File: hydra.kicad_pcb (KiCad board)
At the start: 4 copper layers, 95.9 x 90.2 mm, 61 parts, among them J1 PC104 Interconnect, J2 STLINK/V2 Header, J3 STLINK/V2 Clone Header, J5 UART Header, U2 AMS1117-3.3, U3 STM32F103VCTx, Y1 16mHz

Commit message: feat: trying multinodal
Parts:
- removed the J2 at (160.6, 40.4)
- removed Y1: 16mHz, Crystal:Crystal_HC49-U_Vertical
- added C15: 0.1uF, Capacitor_SMD:C_0603_1608Metric, F.Cu at (168.7, 46.8)
- added C16: 0.1uF, Capacitor_SMD:C_0603_1608Metric, F.Cu at (183.2, 54.6)
- added C17: 0.1uF, Capacitor_SMD:C_0603_1608Metric, F.Cu at (180.3, 60.0)
- added C18: 4.7uF, Capacitor_SMD:C_0603_1608Metric, F.Cu at (139.8, 84.6)
- added C19: 0.1uF, Capacitor_SMD:C_0603_1608Metric, F.Cu at (134.2, 78.3)
- added C20: 0.1uF, Capacitor_SMD:C_0603_1608Metric, F.Cu at (140.2, 90.6)
- added C21: 0.1uF, Capacitor_SMD:C_0603_1608Metric, F.Cu at (122.9, 90.2)
- added C22: 0.1uF, Capacitor_SMD:C_0603_1608Metric, F.Cu at (125.5, 79.8)
- added C23: 0.1uF, Capacitor_SMD:C_0603_1608Metric, F.Cu at (140.0, 87.7)
- added C24: 0.1uF, Capacitor_SMD:C_0603_1608Metric, F.Cu at (137.1, 93.0)
- added C25: 4.7uF, Capacitor_SMD:C_0603_1608Metric, F.Cu at (183.0, 84.6)
- added C26: 0.1uF, Capacitor_SMD:C_0603_1608Metric, F.Cu at (177.4, 78.3)
- added C27: 0.1uF, Capacitor_SMD:C_0603_1608Metric, F.Cu at (183.3, 90.6)
- added C28: 0.1uF, Capacitor_SMD:C_0603_1608Metric, F.Cu at (166.1, 90.2)
- added C29: 0.1uF, Capacitor_SMD:C_0603_1608Metric, F.Cu at (168.7, 79.8)
- added C30: 0.1uF, Capacitor_SMD:C_0603_1608Metric, F.Cu at (183.2, 87.7)
- added C31: 0.1uF, Capacitor_SMD:C_0603_1608Metric, F.Cu at (180.3, 93.0)
- added C32: 4.7uF, Capacitor_SMD:C_0603_1608Metric, F.Cu at (162.6, 110.0)
- added C33: 0.1uF, Capacitor_SMD:C_0603_1608Metric, F.Cu at (157.0, 103.7)
- added C34: 0.1uF, Capacitor_SMD:C_0603_1608Metric, F.Cu at (163.0, 116.0)
- added C35: 0.1uF, Capacitor_SMD:C_0603_1608Metric, F.Cu at (145.8, 115.6)
- added C36: 0.1uF, Capacitor_SMD:C_0603_1608Metric, F.Cu at (148.3, 105.2)
- added C37: 0.1uF, Capacitor_SMD:C_0603_1608Metric, F.Cu at (162.9, 113.1)
- added C38: 0.1uF, Capacitor_SMD:C_0603_1608Metric, F.Cu at (159.9, 118.4)
- added D15: Node Active LED, LED_SMD:LED_0603_1608Metric, F.Cu at (174.0, 45.8)
- added D16: Node Active LED, LED_SMD:LED_0603_1608Metric, F.Cu at (130.8, 78.8)
- added D17: Node Active LED, LED_SMD:LED_0603_1608Metric, F.Cu at (174.0, 78.8)
- added D18: Node Active LED, LED_SMD:LED_0603_1608Metric, F.Cu at (153.7, 104.2)
- added D2: CS1, LED_SMD:LED_0603_1608Metric, F.Cu at (68.1, 90.0)
- added J1: UART Header, Connector_PinHeader_2.54mm:PinHeader_1x03_P2.54mm_Vertical, F.Cu at (74.4, 101.4)
- added J4: STLINK/V2 Clone Header, Connector_PinHeader_2.54mm:PinHeader_2x05_P2.54mm_Vertical, F.Cu at (159.8, 49.8)
- added J6: STLINK/V2 Clone Header, Connector_PinHeader_2.54mm:PinHeader_2x05_P2.54mm_Vertical, F.Cu at (159.8, 82.8)
- added J7: STLINK/V2 Clone Header, Connector_PinHeader_2.54mm:PinHeader_2x05_P2.54mm_Vertical, F.Cu at (139.5, 108.2)
- added R18: 10K, Resistor_SMD:R_0603_1608Metric, F.Cu at (156.0, 121.1)
- added R19: 5.1K, Resistor_SMD:R_0603_1608Metric, F.Cu at (129.8, 43.1)
- added R2: 5.1K, Resistor_SMD:R_0603_1608Metric, F.Cu at (56.0, 97.4)
- added R20: 5.1K, Resistor_SMD:R_0603_1608Metric, F.Cu at (173.0, 43.1)
- added R21: 5.1K, Resistor_SMD:R_0603_1608Metric, F.Cu at (129.8, 76.2)
- added R22: 5.1K, Resistor_SMD:R_0603_1608Metric, F.Cu at (173.0, 76.2)
- added R23: 5.1K, Resistor_SMD:R_0603_1608Metric, F.Cu at (152.7, 101.6)
- added R3: 5.1K, Resistor_SMD:R_0603_1608Metric, F.Cu at (56.0, 99.9)
- added R4: 5.1K, Resistor_SMD:R_0603_1608Metric, F.Cu at (60.0, 87.4)
- added R5: 5.1K, Resistor_SMD:R_0603_1608Metric, F.Cu at (60.0, 89.9)
- added TP12: BOOT1 TP, TestPoint:TestPoint_Pad_D1.0mm, F.Cu at (169.6, 44.4)
- added TP13: BOOT1 TP, TestPoint:TestPoint_Pad_D1.0mm, F.Cu at (126.4, 77.4)
- added TP14: BOOT1 TP, TestPoint:TestPoint_Pad_D1.0mm, F.Cu at (169.6, 77.4)
- added TP15: BOOT1 TP, TestPoint:TestPoint_Pad_D1.0mm, F.Cu at (149.2, 102.8)
- added TP2: PSPI_MOSI_TP, TestPoint:TestPoint_Pad_D1.0mm, F.Cu at (67.5, 103.6)
- added U1: AMS1117-3.3, Package_TO_SOT_SMD:SOT-223-3_TabPin2, F.Cu at (58.9, 105.3)
- added U4: STM32L151RCTx, Package_QFP:LQFP-64_10x10mm_P0.5mm, F.Cu at (131.3, 86.9)
- added U5: STM32L151RCTx, Package_QFP:LQFP-64_10x10mm_P0.5mm, F.Cu at (174.5, 86.9)
- added U6: STM32L151RCTx, Package_QFP:LQFP-64_10x10mm_P0.5mm, F.Cu at (154.2, 112.3)
- C1: value 10uF -> 4.7uF
- C11, C4: value 0.1uF -> 4.7uF
- C2: value 22uF -> 10uF
- C3: value 4.7uF -> 22uF
- C7, C8: value 20pF -> 0.1uF
- D10: value CS8 -> CS9
- D11: value CS9 -> CS10
- D12: value CS10 -> CS11
- D13: value CS11 -> CS12
- D14: value CS12 -> Node Active LED
- D3: value CS1 -> CS2
- D4: value CS2 -> CS3
- D5: value CS3 -> CS4
- D6: value CS4 -> CS5
- D7: value CS5 -> CS6
- D8: value CS6 -> CS7
- D9: value CS7 -> CS8
- J5: value UART Header -> STLINK/V2 Clone Header; footprint Connector_PinHeader_2.54mm:PinHeader_1x03_P2.54mm_Vertical -> Connector_PinHeader_2.54mm:PinHeader_2x05_P2.54mm_Vertical
- R13: footprint Resistor_SMD:R_0603_1608Metric -> Capacitor_SMD:C_0603_1608Metric
- R14, R15, R16: value 5.1K -> 10K
- R17: value 5.1K -> 10K; footprint Capacitor_SMD:C_0603_1608Metric -> Resistor_SMD:R_0603_1608Metric
- TP10: value RSPI_MISO_TP -> RSPI_SCLK_TP
- TP11: value RSPI_SCLK_TP -> BOOT1 TP
- TP3: value PSPI_MOSI_TP -> PSPI_MISO_TP
- TP4: value PSPI_MISO_TP -> PSPI_SCLK_TP
- TP5: value PSPI_SCLK_TP -> SSPI_MOSI_TP
- TP6: value SSPI_MOSI_TP -> SSPI_MISO_TP
- TP7: value SSPI_MISO_TP -> SSPI_SCLK_TP
- TP8: value SSPI_SCLK_TP -> RSPI_MOSI_TP
- TP9: value RSPI_MOSI_TP -> RSPI_MISO_TP
- U2: value AMS1117-3.3 -> STM32L151RCTx; footprint Package_TO_SOT_SMD:SOT-223-3_TabPin2 -> Package_QFP:LQFP-64_10x10mm_P0.5mm
- U3: value STM32F103VCTx -> STM32L151RCTx; footprint Package_QFP:LQFP-100_14x14mm_P0.5mm -> Package_QFP:LQFP-64_10x10mm_P0.5mm
- moved R6 140.4 mm to (60.0, 92.4), turned to 0 degrees
- moved C1 134.2 mm to (56.0, 87.4), turned to 0 degrees
- moved D3 131.4 mm to (68.1, 92.6), turned to 0 degrees
- moved R1 120.7 mm to (56.0, 94.9), turned to 0 degrees
- moved TP9 119.7 mm to (70.6, 109.7)
- moved C2 119.7 mm to (56.0, 89.9), turned to 0 degrees
- moved TP6 119.1 mm to (70.6, 100.6)
- moved TP10 116.9 mm to (70.6, 112.8)
- moved TP7 113.4 mm to (70.6, 103.6)
- moved D1 110.1 mm to (68.1, 87.4), turned to 0 degrees
- moved TP8 108.7 mm to (70.6, 106.7)
- moved R9 108.3 mm to (60.0, 99.9)
- moved TP1 107.1 mm to (67.5, 100.6)
- moved TP5 100.2 mm to (67.5, 112.8)
- moved TP3 94.7 mm to (67.5, 106.7)
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- renumbered H3 to H2, H2 to H3, J1 to J2
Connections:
- C1 pad 1: /3V3_CONN -> +3V3
- C2 pad 1: +3V3 -> /3V3_CONN
- C7 pad 1: GND -> +3V3
- C7 pad 2: /OSC+ -> GND
- C8 pad 1: GND -> +3V3
- C8 pad 2: /OSC- -> GND
- C9 pad 1: /RESET -> /Node/RESET
- D10 pad 2: /CS_8 -> /CS_9
- D11 pad 2: /CS_9 -> /CS_10
- D12 pad 2: /CS_10 -> /CS_11
- D13 pad 2: /CS_11 -> /CS_12
- D14 pad 2: /CS_12 -> Net-(D14-A)
- D3 pad 2: /CS_1 -> /CS_2
- D4 pad 2: /CS_2 -> /CS_3
- D5 pad 2: /CS_3 -> /CS_4
- D6 pad 2: /CS_4 -> /CS_5
- D7 pad 2: /CS_5 -> /CS_6
- D8 pad 2: /CS_6 -> /CS_7
- D9 pad 2: /CS_7 -> /CS_8
- J2 pad 32: /JTDO/R_SCLK -> /R_SCLK
- J2 pad 34: /NJTRST/R_MISO -> /R_MISO
- J3 pad 1: /RESET -> /Node/RESET
- J3 pad 2: GND -> /Node/SWDIO
- J3 pad 3: /SWIM -> GND
- J3 pad 4: +3V3 -> GND
- J3 pad 6: /JTMS/SWDIO -> /Node/SWCLK
- J3 pad 7: GND -> +3V3
- J3 pad 8: /JTCK/SWCLK -> +3V3
- J3 pad 9: +3V3 -> unconnected-(J3-Pin_9-Pad9)
- J5 pad 1: /USART_RX -> /Node2/RESET
- J5 pad 2: /USART_TX -> /Node2/SWDIO
- R10 pad 2: Net-(D7-K) -> Net-(D10-K)
- R11 pad 2: Net-(D8-K) -> Net-(D11-K)
- R12 pad 2: Net-(D9-K) -> Net-(D12-K)
- R13 pad 2: Net-(D10-K) -> Net-(D13-K)
- R14 pad 2: Net-(D11-K) -> Net-(U2-BOOT0)
- R15 pad 2: Net-(D12-K) -> Net-(U3-BOOT0)
- R16 pad 2: Net-(D13-K) -> Net-(U4-BOOT0)
- R17 pad 2: Net-(D14-K) -> Net-(U5-BOOT0)
- R6 pad 2: Net-(D3-K) -> Net-(D6-K)
- R7 pad 2: Net-(D4-K) -> Net-(D7-K)
- R8 pad 2: Net-(D5-K) -> Net-(D8-K)
- R9 pad 2: Net-(D6-K) -> Net-(D9-K)
- TP10 pad 1: /NJTRST/R_MISO -> /R_SCLK
- TP11 pad 1: /JTDO/R_SCLK -> /Node/BOOT1
- TP3 pad 1: /P_MOSI -> /P_MISO
- TP4 pad 1: /P_MISO -> /P_SCLK
- TP5 pad 1: /P_SCLK -> /S_MOSI
- TP6 pad 1: /S_MOSI -> /S_MISO
- TP7 pad 1: /S_MISO -> /S_SCLK
- TP8 pad 1: /S_SCLK -> /R_MOSI
- TP9 pad 1: /R_MOSI -> /R_MISO
- U2 pad 1: GND -> +3V3
- U2 pad 2: +3V3 -> /CS_12
- U2 pad 3: /3V3_CONN -> /CS_11
- U3 pad 1: unconnected-(U3-PE2-Pad1) -> +3V3
- U3 pad 10: GND -> /CS_7
- U3 pad 11: +3V3 -> /CS_6
- U3 pad 12: /OSC+ -> GND
- U3 pad 13: /OSC- -> +3V3
- U3 pad 14: /RESET -> /CS_5
- U3 pad 15: unconnected-(U3-PC0-Pad15) -> /CS_4
- U3 pad 16: unconnected-(U3-PC1-Pad16) -> /CS_3
- U3 pad 17: unconnected-(U3-PC2-Pad17) -> /CS_2
- U3 pad 18: unconnected-(U3-PC3-Pad18) -> GND
- U3 pad 19: GND -> +3V3
- U3 pad 2: unconnected-(U3-PE3-Pad2) -> /CS_12
- U3 pad 20: GND -> /CS_1
- U3 pad 21: +3V3 -> /P_SCLK
- U3 pad 22: +3V3 -> /P_MISO
- U3 pad 23: unconnected-(U3-PA0-Pad23) -> /P_MOSI
- U3 pad 24: unconnected-(U3-PA1-Pad24) -> Net-(D15-A)
- U3 pad 27: GND -> unconnected-(U3-PB1-Pad27)
- U3 pad 28: +3V3 -> /Node1/BOOT1
- U3 pad 3: unconnected-(U3-PE4-Pad3) -> /CS_11
- U3 pad 30: /P_SCLK -> unconnected-(U3-PB11-Pad30)
- U3 pad 31: /P_MISO -> GND
- U3 pad 32: /P_MOSI -> +3V3
- U3 pad 34: unconnected-(U3-PC5-Pad34) -> /S_SCLK
- U3 pad 35: unconnected-(U3-PB0-Pad35) -> /S_MISO
- U3 pad 36: unconnected-(U3-PB1-Pad36) -> /S_MOSI
- U3 pad 4: unconnected-(U3-PE5-Pad4) -> /CS_10
- U3 pad 46: unconnected-(U3-PE15-Pad46) -> /Node1/SWDIO
- U3 pad 47: unconnected-(U3-PB10-Pad47) -> GND
- U3 pad 48: unconnected-(U3-PB11-Pad48) -> +3V3
- U3 pad 49: GND -> /Node1/SWCLK
- U3 pad 50: +3V3 -> unconnected-(U3-PA15-Pad50)
- U3 pad 51: unconnected-(U3-PB12-Pad51) -> /R_SCLK
- U3 pad 52: /S_SCLK -> /R_MISO
- U3 pad 53: /S_MISO -> /R_MOSI
- U3 pad 54: /S_MOSI -> /R_CS
- U3 pad 55: /R_CS -> /Node1/JTDO
- U3 pad 56: /CS_12 -> /Node1/NJTRST
- U3 pad 57: /CS_11 -> unconnected-(U3-PB5-Pad57)
- U3 pad 58: /CS_10 -> /USART_TX
- U3 pad 59: /CS_9 -> /USART_RX
- U3 pad 6: +3V3 -> unconnected-(U3-PH1-Pad6)
- U3 pad 60: /CS_8 -> Net-(U3-BOOT0)
- U3 pad 61: /CS_7 -> /INTRA_SCL
- U3 pad 62: /CS_6 -> /INTRA_SDA
- U3 pad 63: /CS_5 -> GND
- U3 pad 64: /CS_4 -> +3V3
- U3 pad 7: unconnected-(U3-PC13-Pad7) -> /Node1/RESET
- U3 pad 8: unconnected-(U3-PC14-Pad8) -> /CS_9
- U3 pad 9: unconnected-(U3-PC15-Pad9) -> /CS_8
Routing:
- net /S_MOSI: track 55.0 -> 192.6 mm, vias 2 -> 12
- net /S_MISO: track 57.1 -> 193.2 mm, vias 2 -> 13
- net /S_SCLK: track 55.7 -> 191.6 mm, vias 3 -> 12
- net /P_SCLK: track 65.4 -> 179.8 mm, vias 0 -> 5
- net /NJTRST/R_MISO: track 112.8 -> 0.00 mm, vias 3 -> 0
- net /JTDO/R_SCLK: track 109.9 -> 0.00 mm, vias 4 -> 0
- net /P_MOSI: track 63.0 -> 170.9 mm, vias 0 -> 8
- net /P_MISO: track 66.7 -> 172.2 mm, vias 0 -> 7
- net /RESET: track 86.7 -> 0.00 mm
- net GND: track 18.7 -> 98.6 mm, vias 48 -> 46
- net /JTCK/SWCLK: track 69.1 -> 0.00 mm, vias 2 -> 0
- net /R_CS: track 69.0 -> 0.00 mm
- net /R_MOSI: track 66.9 -> 0.00 mm, vias 2 -> 0
- net /JTMS/SWDIO: track 66.0 -> 0.00 mm
- net /CS_12: track 56.6 -> 118.1 mm, vias 0 -> 1
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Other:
- board text removed: "(0, 0) local"
- board text removed: "(205, 125) world"

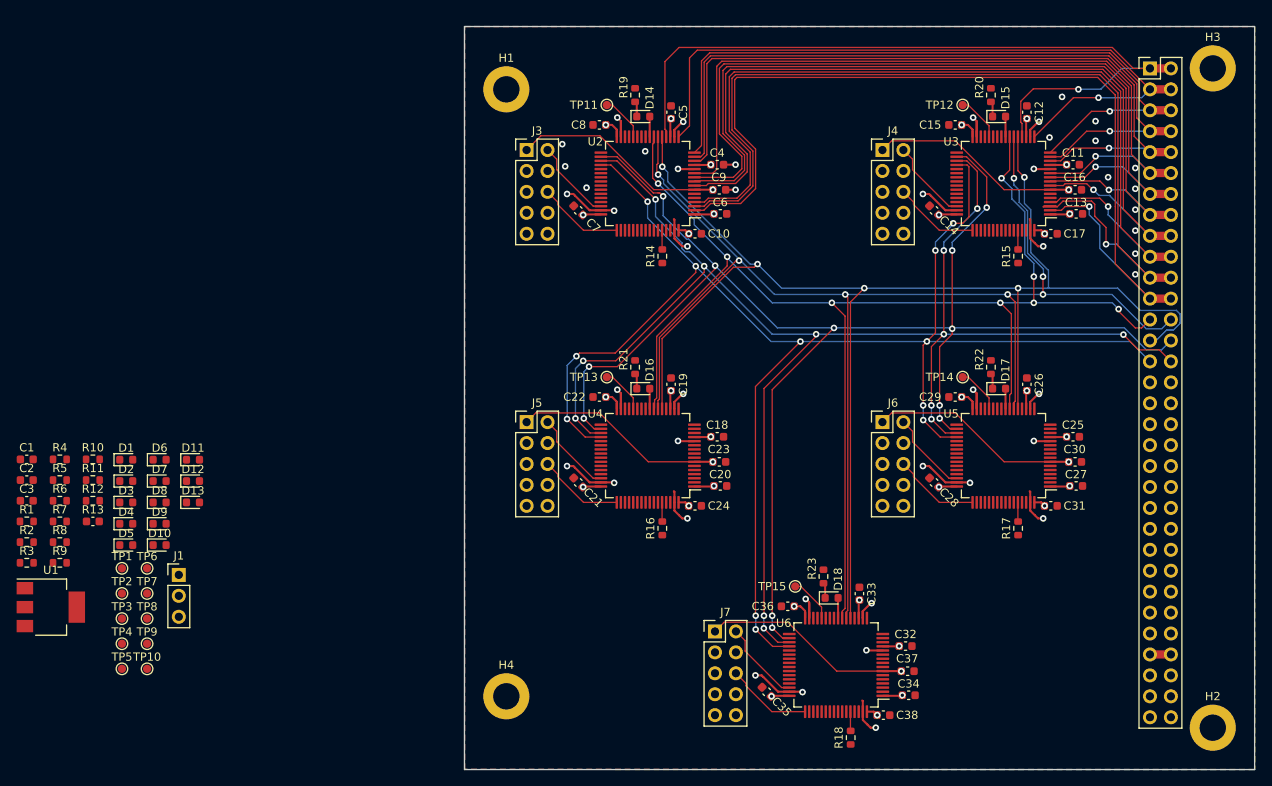
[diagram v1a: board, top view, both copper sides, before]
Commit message: feat: more routing
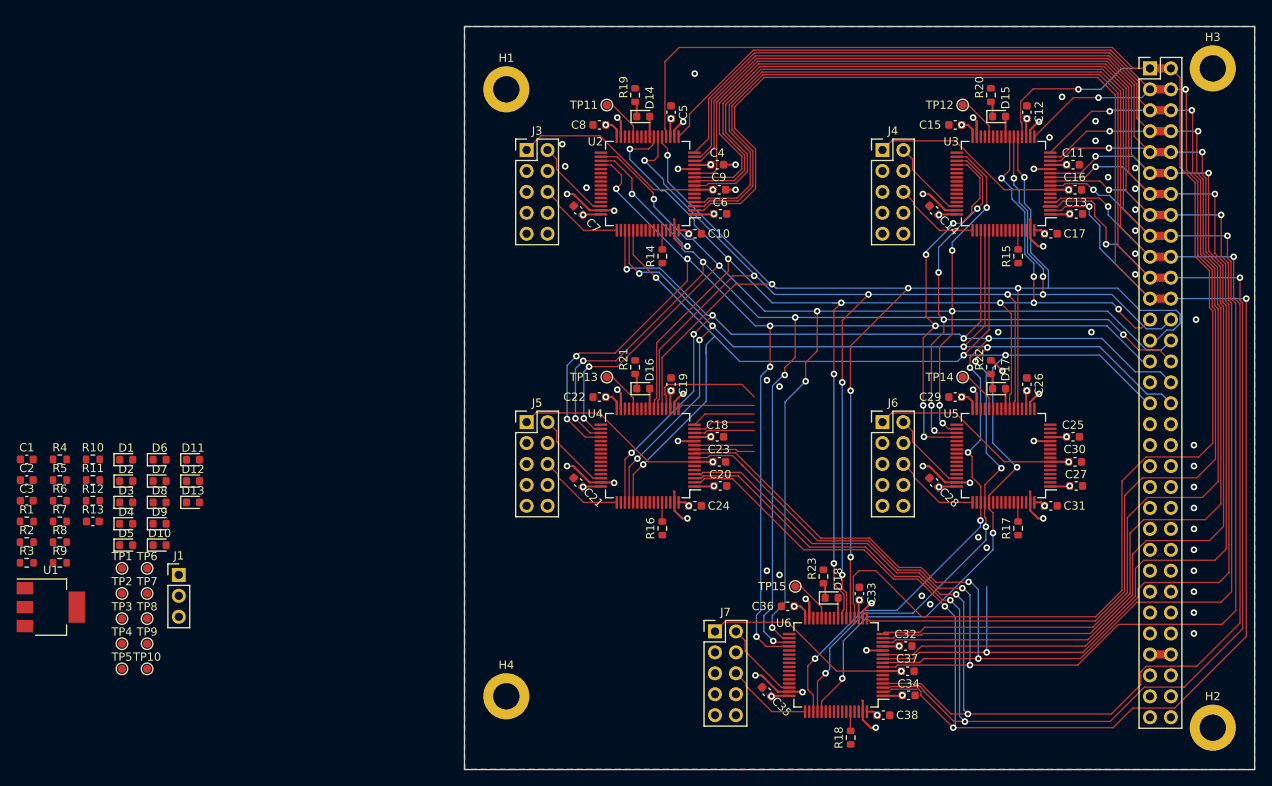
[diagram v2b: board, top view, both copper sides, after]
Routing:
- net /R_SCLK: track 0.00 -> 177.2 mm, vias 0 -> 10
- net /R_MISO: track 0.00 -> 176.8 mm, vias 0 -> 10
- net /R_MOSI: track 0.00 -> 174.7 mm, vias 0 -> 7
- net /CS_10: track 110.4 -> 264.3 mm, vias 1 -> 4
- net /CS_12: track 118.1 -> 271.1 mm, vias 1 -> 4
- net /CS_11: track 116.8 -> 269.4 mm, vias 1 -> 4
- net /CS_8: track 103.0 -> 248.8 mm, vias 1 -> 4
- net /CS_9: track 106.0 -> 251.5 mm, vias 1 -> 4
- net /CS_1: track 94.1 -> 223.8 mm
- net /CS_7: track 101.1 -> 213.4 mm, vias 1 -> 3
- net /CS_2: track 87.3 -> 198.3 mm, vias 1 -> 2
- net /CS_3: track 87.2 -> 194.4 mm, vias 1 -> 2
- net /CS_4: track 89.0 -> 195.3 mm, vias 1 -> 2
- net /CS_5: track 90.8 -> 195.4 mm, vias 1 -> 2
- net /CS_6: track 95.2 -> 199.7 mm, vias 1 -> 2
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- added copper zone on B.Cu, net +3V3
- added copper zone on In2.Cu, net GND
- removed copper zone on In2.Cu, net +3V3
- removed copper zone on B.Cu, net GND

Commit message: feat: mostly put together multinode
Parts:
- added G***: LOGO, mod:hsl, F.Cu at (126.8, 107.5)
- added kibuzzard-65E1979C: G***, kibuzzard-65E1979C, F.Cu at (138.8, 47.8)
- added kibuzzard-65E197AB: G***, kibuzzard-65E197AB, F.Cu at (182.3, 46.9)
- added kibuzzard-65E197B8: G***, kibuzzard-65E197B8, F.Cu at (138.2, 80.8)
- added kibuzzard-65E197C4: G***, kibuzzard-65E197C4, F.Cu at (182.5, 80.9)
- added kibuzzard-65E197D2: G***, kibuzzard-65E197D2, F.Cu at (161.6, 106.2)
- added kibuzzard-65E19948: G***, kibuzzard-65E19948, F.Cu at (127.0, 117.6)
- moved C2 135.0 mm to (189.5, 110.2), turned to 90 degrees
- moved U1 125.3 mm to (183.9, 113.3), turned to 180 degrees
- moved C3 124.4 mm to (178.7, 112.6), turned to 90 degrees
- moved TP10 123.8 mm to (189.0, 76.7)
- moved TP9 119.4 mm to (185.2, 76.1)
- moved TP8 114.3 mm to (180.4, 74.7)
- moved TP7 105.5 mm to (168.3, 63.8)
- moved TP4 101.8 mm to (160.8, 68.9)
- moved TP3 96.4 mm to (156.4, 69.1)
- moved TP2 91.7 mm to (153.9, 73.1)
- moved TP5 87.5 mm to (146.2, 74.5)
- moved TP6 83.3 mm to (149.2, 73.1)
- moved C1 4.40 mm to (56.1, 83.0)
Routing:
- net /INTRA_SCL: track 0.00 -> 209.4 mm, vias 0 -> 13
- net /INTRA_SDA: track 0.00 -> 208.3 mm, vias 0 -> 10
- net /R_CS: track 0.00 -> 160.4 mm, vias 0 -> 9
- net /CS_1: track 223.8 -> 295.2 mm
- net /CS_2: track 198.3 -> 263.3 mm, vias 2 -> 6
- net /CS_5: track 195.4 -> 259.0 mm, vias 2 -> 6
- net /CS_4: track 195.3 -> 258.2 mm, vias 2 -> 6
- net /CS_3: track 194.4 -> 256.5 mm, vias 2 -> 6
- net /CS_6: track 199.7 -> 259.7 mm, vias 2 -> 6
- net /CS_7: track 213.4 -> 264.9 mm, vias 3 -> 6
- net /CS_12: track 271.1 -> 297.3 mm, vias 4 -> 6
- net /CS_11: track 269.4 -> 294.9 mm, vias 4 -> 6
- net /CS_10: track 264.3 -> 289.4 mm, vias 4 -> 6
- net /CS_9: track 251.5 -> 272.7 mm, vias 4 -> 6
- net /CS_8: track 248.8 -> 266.7 mm, vias 4 -> 6
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- added copper zone on In2.Cu, net +3V3
- added copper zone on B.Cu, net GND
- removed copper zone on B.Cu, net +3V3
- removed copper zone on In2.Cu, net GND

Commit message: feat: in progress rework
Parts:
- removed C1, C11, C18, C25, C32: 4.7uF, Capacitor_SMD:C_0603_1608Metric
- removed C12, C13, C14, C15, C16, C17, C19, C20, C21, C22, C23, C24, C26, C27, C28, C29, C30, C31, C33, C34, C35, C36, C37, C38: 0.1uF, Capacitor_SMD:C_0603_1608Metric
- removed D10: CS9, LED_SMD:LED_0603_1608Metric
- removed D11: CS10, LED_SMD:LED_0603_1608Metric
- removed D12: CS11, LED_SMD:LED_0603_1608Metric
- removed D13: CS12, LED_SMD:LED_0603_1608Metric
- removed D14, D15, D16, D17, D18: Node Active LED, LED_SMD:LED_0603_1608Metric
- removed D2: CS1, LED_SMD:LED_0603_1608Metric
- removed D3: CS2, LED_SMD:LED_0603_1608Metric
- removed D4: CS3, LED_SMD:LED_0603_1608Metric
- removed D5: CS4, LED_SMD:LED_0603_1608Metric
- removed D6: CS5, LED_SMD:LED_0603_1608Metric
- removed D7: CS6, LED_SMD:LED_0603_1608Metric
- removed D8: CS7, LED_SMD:LED_0603_1608Metric
- removed D9: CS8, LED_SMD:LED_0603_1608Metric
- removed J1: UART Header, Connector_PinHeader_2.54mm:PinHeader_1x03_P2.54mm_Vertical
- removed J4, J5, J6, J7: STLINK/V2 Clone Header, Connector_PinHeader_2.54mm:PinHeader_2x05_P2.54mm_Vertical
- removed R10, R11, R12, R19, R2, R20, R21, R22, R23, R3, R4, R5, R6, R7, R8, R9: 5.1K, Resistor_SMD:R_0603_1608Metric
- removed R13: 5.1K, Capacitor_SMD:C_0603_1608Metric
- removed R14, R15, R16, R17, R18: 10K, Resistor_SMD:R_0603_1608Metric
- removed TP12, TP13, TP14, TP15: BOOT1 TP, TestPoint:TestPoint_Pad_D1.0mm
- removed U4, U5, U6: STM32L151RCTx, Package_QFP:LQFP-64_10x10mm_P0.5mm
- removed kibuzzard-65E1979C: G***, kibuzzard-65E1979C
- removed kibuzzard-65E197AB: G***, kibuzzard-65E197AB
- removed kibuzzard-65E197B8: G***, kibuzzard-65E197B8
- removed kibuzzard-65E197C4: G***, kibuzzard-65E197C4
- removed kibuzzard-65E197D2: G***, kibuzzard-65E197D2
- added J8: TC2030, Connector:Tag-Connect_TC2030-IDC-FP_2x03_P1.27mm_Vertical, F.Cu at (166.6, 47.0)
- J3: value STLINK/V2 Clone Header -> USB-C; footprint Connector_PinHeader_2.54mm:PinHeader_2x05_P2.54mm_Vertical -> Connector_USB:USB_C_Receptacle_G-Switch_GT-USB-7010ASV
- U2: value STM32L151RCTx -> STM32L151RCT6
- U3: value STM32L151RCTx -> USBLC6-2SC6; footprint Package_QFP:LQFP-64_10x10mm_P0.5mm -> Package_TO_SOT_SMD:SOT-23-6
- moved C2 84.1 mm to (122.4, 59.4), turned to 0 degrees
- moved C3 75.7 mm to (122.4, 61.9), turned to 0 degrees
- moved R1 73.1 mm to (122.4, 64.4)
- moved D1 72.1 mm to (134.5, 59.4)
- moved TP1 72.1 mm to (134.0, 72.6)
- moved U1 68.7 mm to (125.4, 77.4), turned to 0 degrees
- moved J3 59.3 mm to (174.7, 37.5), turned to 180 degrees
- moved TP10 52.6 mm to (137.0, 84.8)
- moved TP9 48.5 mm to (137.0, 81.8)
- moved U2 45.3 mm to (176.6, 55.8), turned to 90 degrees
- moved TP8 43.5 mm to (137.0, 78.7)
- moved TP5 42.9 mm to (187.5, 62.9)
- moved C5 41.9 mm to (172.0, 63.3), turned to 180 degrees
- moved TP11 39.4 mm to (148.1, 77.2)
- moved TP2 39.0 mm to (181.0, 44.9)
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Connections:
- U2 pad 10: /CS_7 -> unconnected-(U2-PC2-Pad10)
- U2 pad 11: /CS_6 -> /R_CS
- U2 pad 14: /CS_5 -> /CS_12
- U2 pad 15: /CS_4 -> /CS_11
- U2 pad 16: /CS_3 -> /CS_10
- U2 pad 17: /CS_2 -> /CS_9
- U2 pad 2: /CS_12 -> unconnected-(U2-PC13-Pad2)
- U2 pad 20: /CS_1 -> /CS_8
- U2 pad 21: /P_SCLK -> /S_SCLK
- U2 pad 22: /P_MISO -> /S_MISO
- U2 pad 23: /P_MOSI -> /S_MOSI
- U2 pad 24: Net-(D14-A) -> /CS_7
- U2 pad 25: unconnected-(U2-PC5-Pad25) -> /CS_6
- U2 pad 26: unconnected-(U2-PB0-Pad26) -> /CS_5
- U2 pad 27: unconnected-(U2-PB1-Pad27) -> /CS_4
- U2 pad 29: unconnected-(U2-PB10-Pad29) -> /CS_3
- U2 pad 3: /CS_11 -> unconnected-(U2-PC14-Pad3)
- U2 pad 30: unconnected-(U2-PB11-Pad30) -> /CS_2
- U2 pad 33: unconnected-(U2-PB12-Pad33) -> /CS_1
- U2 pad 34: /S_SCLK -> /P_SCLK
- U2 pad 35: /S_MISO -> /P_MISO
- U2 pad 36: /S_MOSI -> /P_MOSI
- U2 pad 4: /CS_10 -> unconnected-(U2-PC15-Pad4)
- U2 pad 44: unconnected-(U2-PA11-Pad44) -> /Node/USB_D-
- U2 pad 45: unconnected-(U2-PA12-Pad45) -> /Node/USB_D+
- U2 pad 46: /Node/SWDIO -> /Node/SWD_IO
- U2 pad 49: /Node/SWCLK -> /Node/SWD_CLK
- U2 pad 5: unconnected-(U2-PH0-Pad5) -> /Node/HSE+
- U2 pad 54: /R_CS -> unconnected-(U2-PD2-Pad54)
- U2 pad 55: /Node/JTDO -> unconnected-(U2-PB3-Pad55)
- U2 pad 56: /Node/NJTRST -> unconnected-(U2-PB4-Pad56)
- U2 pad 58: /USART_TX -> /Node/UART_RX
- U2 pad 59: /USART_RX -> /Node/UART_TX
- U2 pad 6: unconnected-(U2-PH1-Pad6) -> /Node/HSE-
- U2 pad 60: Net-(U2-BOOT0) -> /Node/BOOT0
- U2 pad 8: /CS_9 -> unconnected-(U2-PC0-Pad8)
- U2 pad 9: /CS_8 -> unconnected-(U2-PC1-Pad9)
- U3 pad 1: +3V3 -> /Node/USB_DT-
- U3 pad 2: /CS_12 -> GND
- U3 pad 3: /CS_11 -> /Node/USB_DT+
- U3 pad 4: /CS_10 -> /Node/USB_D+
- U3 pad 5: unconnected-(U3-PH0-Pad5) -> Net-(U3-VBUS)
- U3 pad 6: unconnected-(U3-PH1-Pad6) -> /Node/USB_D-
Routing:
- net /CS_12: track 297.3 -> 19.3 mm, vias 6 -> 1
- net /CS_11: track 294.9 -> 17.6 mm, vias 6 -> 1
- net /CS_1: track 295.2 -> 18.8 mm
- net /CS_10: track 289.4 -> 15.9 mm, vias 6 -> 1
- net /CS_9: track 272.7 -> 12.8 mm, vias 6 -> 1
- net /CS_8: track 266.7 -> 13.3 mm, vias 6 -> 1
- net /CS_7: track 264.9 -> 12.9 mm, vias 6 -> 1
- net /CS_6: track 259.7 -> 13.8 mm, vias 6 -> 1
- net /CS_2: track 263.3 -> 18.5 mm, vias 6 -> 1
- net /CS_5: track 259.0 -> 14.6 mm, vias 6 -> 1
- net /CS_4: track 258.2 -> 15.5 mm, vias 6 -> 1
- net /CS_3: track 256.5 -> 17.3 mm, vias 6 -> 1
- net /INTRA_SCL: track 209.4 -> 0.00 mm, vias 13 -> 0
- net /INTRA_SDA: track 208.3 -> 0.00 mm, vias 10 -> 0
- net /S_MOSI: track 197.7 -> 25.8 mm, vias 12 -> 0
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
